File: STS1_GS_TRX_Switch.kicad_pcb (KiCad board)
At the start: 4 copper layers, 101 x 65 mm, 60 parts, among them J1 SDR, J10 PA_Switch, J11 LNA_Switch, J2 From_LNA, J3 To_PA, J4 To_LNA, J5 From_PA, J6 Antenna, J7 RX_LED, J8 TX_LED, J9 5V_Supply, K1 HF3-53, K2 HF3-53, K3 HF3-53, K4 IM07, K5 IM07, Q1 BC847, Q2 BC847, Q3 BC847, Q4 BC847, Q5 BC847, U1 PC817, U2 PC817

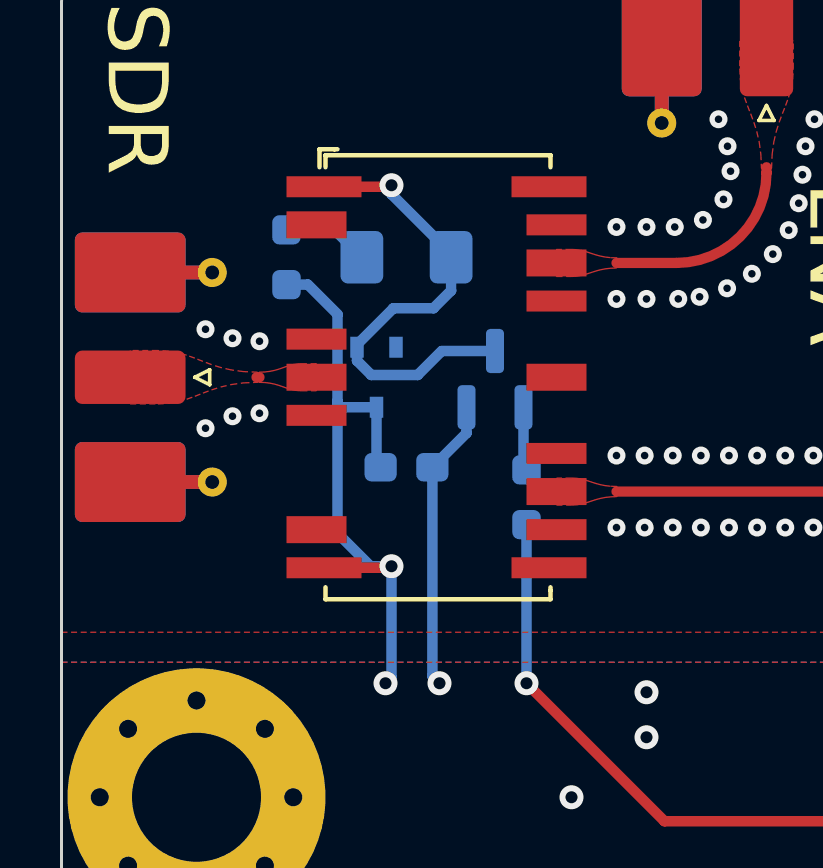
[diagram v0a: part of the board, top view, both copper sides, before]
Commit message: fix: wrong polarity of one of the RF relays
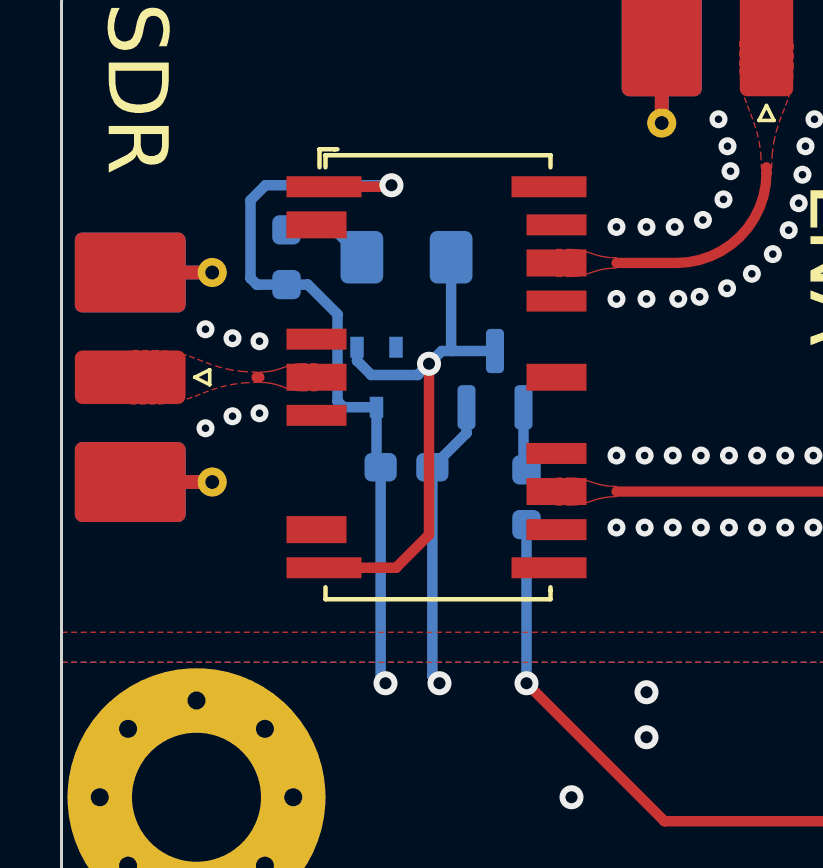
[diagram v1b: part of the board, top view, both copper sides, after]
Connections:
- K1 pad 1: Net-(D1-A) -> +5V
- K1 pad 11: +5V -> Net-(D1-A)
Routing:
- net +5V: track 123.7 -> 128.8 mm
- net Net-(D1-A): track 16.2 -> 18.5 mm

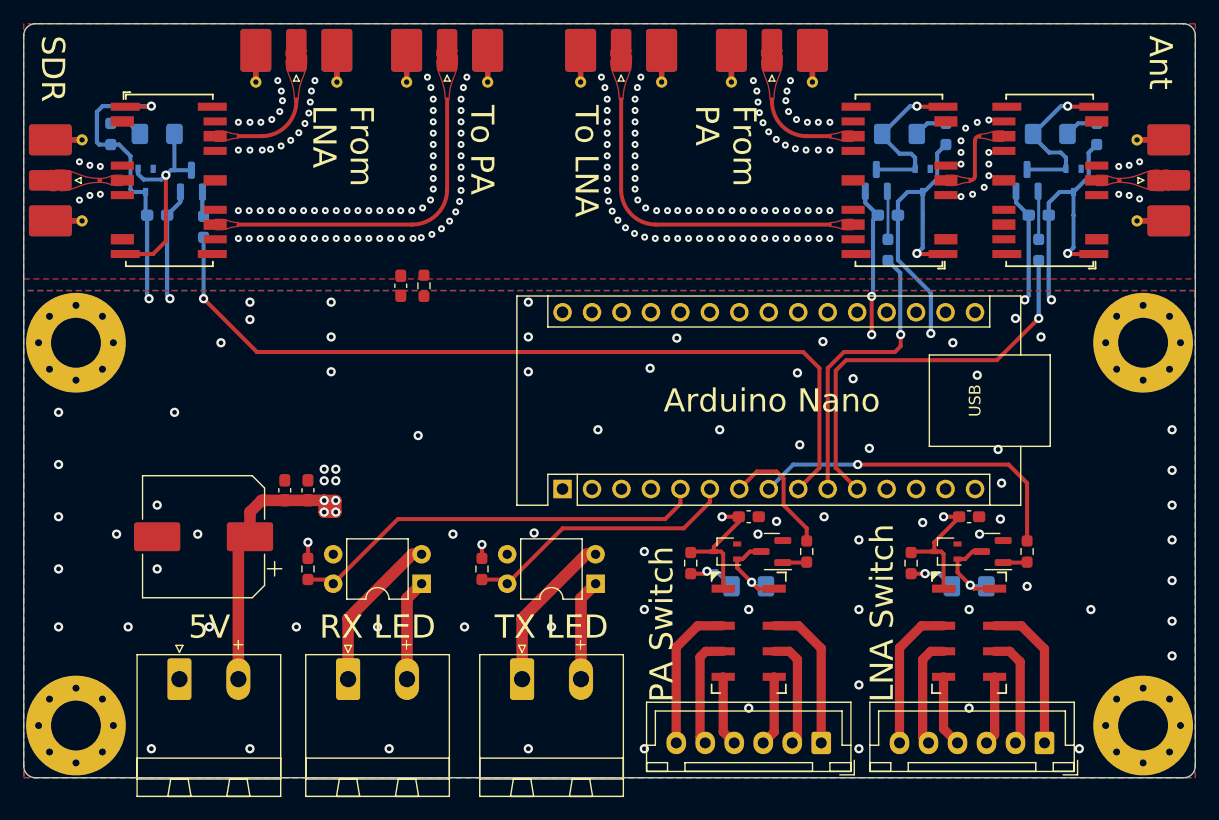
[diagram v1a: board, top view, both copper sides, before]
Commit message: feat: v2.0 with built-in LNA, PA-pre-filter and PA output filter
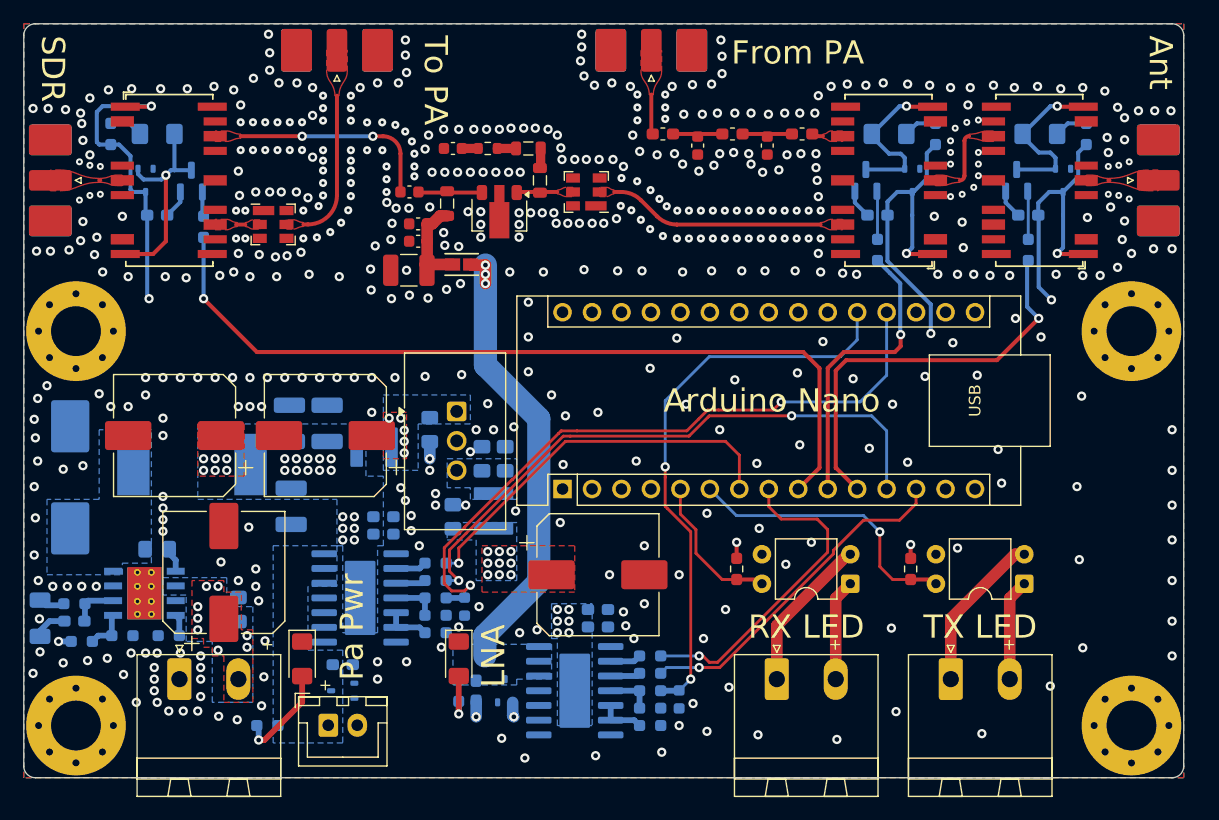
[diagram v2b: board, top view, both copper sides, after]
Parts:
- removed C2: 100µ, Capacitor_SMD:CP_Elec_10x10
- removed C3: 100n, Capacitor_SMD:C_0603_1608Metric_Pad1.08x0.95mm_HandSolder
- removed D10: LNA_Sw, LED_SMD:LED_1206_3216Metric_Pad1.42x1.75mm_HandSolder
- removed J10: PA_Switch, Connector_JST:JST_XH_B6B-XH-A_1x06_P2.50mm_Vertical
- removed J11: LNA_Switch, Connector_JST:JST_XH_B6B-XH-A_1x06_P2.50mm_Vertical
- removed J4: To_LNA, Connector_Coaxial:SMA_Molex_73251-2120_EdgeMount_Horizontal
- removed K4, K5: IM07, Relay_SMD:Relay_DPDT_AXICOM_IMSeries_JLeg
- removed Q4, Q5: BC847, Package_TO_SOT_SMD:SOT-23
- removed R7: 10k, Resistor_SMD:R_0603_1608Metric_Pad0.98x0.95mm_HandSolder
- added C10: 330pF, Capacitor_SMD:C_0603_1608Metric, F.Cu at (144.5, 56.2)
- added C11: 100pF, Capacitor_SMD:C_0603_1608Metric, F.Cu at (141.5, 62.8)
- added C12: 100nF, Capacitor_SMD:C_0603_1608Metric, F.Cu at (141.5, 64.2)
- added C14: 100pF, Capacitor_SMD:C_0603_1608Metric, F.Cu at (140.8, 60.0)
- added C15: 7.5pF, Capacitor_SMD:C_0603_1608Metric, F.Cu at (165.6, 56.0)
- added C16: 7.5pF, Capacitor_SMD:C_0603_1608Metric, F.Cu at (171.6, 56.0)
- added C17: 100pF, Capacitor_SMD:C_0603_1608Metric, B.Cu at (145.5, 95.8)
- added C18: 100pF, Capacitor_SMD:C_0603_1608Metric, B.Cu at (164.0, 103.8)
- added C19: 1µ, Capacitor_SMD:C_0603_1608Metric_Pad1.08x0.95mm_HandSolder, B.Cu at (157.0, 96.0)
- added C20: 1µ, Capacitor_SMD:C_0603_1608Metric_Pad1.08x0.95mm_HandSolder, B.Cu at (157.0, 97.5)
- added C21: 1µ, Capacitor_SMD:C_0603_1608Metric_Pad1.08x0.95mm_HandSolder, B.Cu at (146.5, 103.0)
- added C22: 100µ, Capacitor_SMD:CP_Elec_10x10, F.Cu at (133.5, 81.0)
- added C23: 10µ, Capacitor_SMD:C_0805_2012Metric_Pad1.18x1.45mm_HandSolder, B.Cu at (142.5, 80.5)
- added C24: 10µ, Capacitor_SMD:C_1210_3225Metric_Pad1.33x2.70mm_HandSolder, B.Cu at (130.6, 87.1)
- added C25: 10µ, Capacitor_SMD:C_1210_3225Metric_Pad1.33x2.70mm_HandSolder, B.Cu at (133.7, 80.0)
- added C26: 10µ, Capacitor_SMD:C_0805_2012Metric_Pad1.18x1.45mm_HandSolder, B.Cu at (147.0, 83.0)
- added C27: 10µ, Capacitor_SMD:C_0805_2012Metric_Pad1.18x1.45mm_HandSolder, B.Cu at (149.0, 83.0)
- added C28: 10µ, Capacitor_SMD:C_0805_2012Metric_Pad1.18x1.45mm_HandSolder, B.Cu at (144.5, 88.0)
- added C29: 100µ, Capacitor_SMD:CP_Elec_10x10, F.Cu at (157.0, 93.0)
- added C30: 100µ, Capacitor_SMD:CP_Elec_10x10, F.Cu at (124.8, 92.8)
- added C31: 10µ, Capacitor_SMD:C_0805_2012Metric_Pad1.18x1.45mm_HandSolder, B.Cu at (126.0, 96.0)
- added C32: 100n, Capacitor_SMD:C_0805_2012Metric_Pad1.18x1.45mm_HandSolder, B.Cu at (119.0, 90.8)
- added C33: 100p, Capacitor_SMD:C_0603_1608Metric_Pad1.08x0.95mm_HandSolder, B.Cu at (111.9, 97.0)
- added C34: 7.5n, Capacitor_SMD:C_1206_3216Metric_Pad1.33x1.80mm_HandSolder, B.Cu at (108.9, 96.8)
- added C35: 100µ, Capacitor_SMD:CP_Elec_10x10, F.Cu at (120.5, 81.0)
- added C36: 10µ, Capacitor_SMD:C_1210_3225Metric_Pad1.33x2.70mm_HandSolder, B.Cu at (130.4, 80.0)
- added D11: LNA_Sw, LED_SMD:LED_1206_3216Metric_Pad1.42x1.75mm_HandSolder, F.Cu at (145.0, 100.2)
- added D12: CDBC560-G, Diode_SMD:D_SMC_Handsoldering, B.Cu at (111.5, 84.6)
- added FB1: 600R/0.5A, fbead:Murata-BLM18-0.15-t0.8-0-0-IPC_A, F.Cu at (145.2, 66.2)
- added L1: 33nH, Inductor_SMD:L_0603_1608Metric_Pad1.05x0.95mm_HandSolder, F.Cu at (162.6, 55.0)
- added L2: 51nH, Inductor_SMD:L_0603_1608Metric_Pad1.05x0.95mm_HandSolder, F.Cu at (168.6, 55.0)
- added L3: 220nH, Inductor_SMD:L_0805_2012Metric, F.Cu at (152.0, 59.0)
- added L4: 390nH, Inductor_SMD:L_0805_2012Metric, F.Cu at (151.0, 56.2)
- added L5: 220nH, Inductor_SMD:L_0805_2012Metric, F.Cu at (144.0, 61.0)
- added L6: 33nH, Inductor_SMD:L_0603_1608Metric_Pad1.05x0.95mm_HandSolder, F.Cu at (174.6, 55.0)
- added L7: 5.6µH, Inductor_SMD:L_Abracon_ASPI-4030S, B.Cu at (137.7, 82.0)
- added L8: 5.6µH, Inductor_SMD:L_Abracon_ASPI-4030S, B.Cu at (148.0, 87.5)
- added L9: 27µH, Inductor_SMD:L_Bourns_SRR1210A, B.Cu at (122.0, 83.5)
- added R14: 120, Resistor_SMD:R_0603_1608Metric, F.Cu at (147.5, 56.2)
- added R15: 10k, Resistor_SMD:R_0603_1608Metric_Pad0.98x0.95mm_HandSolder, B.Cu at (143.0, 92.0)
- added R16: 10k, Resistor_SMD:R_0603_1608Metric_Pad0.98x0.95mm_HandSolder, B.Cu at (161.5, 103.0)
- added R17: 10k, Resistor_SMD:R_0603_1608Metric_Pad0.98x0.95mm_HandSolder, B.Cu at (143.0, 93.5)
- added R18: 1.8k, Resistor_SMD:R_0603_1608Metric_Pad0.98x0.95mm_HandSolder, B.Cu at (161.5, 104.5)
- added R19: 10k, Resistor_SMD:R_0603_1608Metric_Pad0.98x0.95mm_HandSolder, B.Cu at (143.0, 95.0)
- added R20: 1.8k, Resistor_SMD:R_0603_1608Metric_Pad0.98x0.95mm_HandSolder, B.Cu at (143.0, 96.5)
- added R21: 10k, Resistor_SMD:R_0603_1608Metric_Pad0.98x0.95mm_HandSolder, B.Cu at (161.5, 106.0)
- added R22: 10k, Resistor_SMD:R_0603_1608Metric_Pad0.98x0.95mm_HandSolder, B.Cu at (145.0, 103.0)
- added R23: 221k, Resistor_SMD:R_0603_1608Metric_Pad0.98x0.95mm_HandSolder, B.Cu at (120.0, 98.2)
- added R24: 221k, Resistor_SMD:R_0603_1608Metric_Pad0.98x0.95mm_HandSolder, B.Cu at (111.9, 95.5)
- added R25: 370k, Resistor_SMD:R_0603_1608Metric_Pad0.98x0.95mm_HandSolder, B.Cu at (112.5, 98.8)
- added R26: 11k, Resistor_SMD:R_0603_1608Metric_Pad0.98x0.95mm_HandSolder, B.Cu at (116.0, 98.2)
- added U3: PGA-103+, Package_TO_SOT_SMD:SOT-89-3, F.Cu at (148.5, 62.0)
- added U4: BTT6050-2EKA, btt6050-2eka:Infineon_PG-DSO-14-40-EP_3.9x8.65mm_P1.27mm, B.Cu at (136.5, 95.0)
- added U5: TSR2-2450, Converter_DCDC:Converter_DCDC_TRACO_TSR2-xxxx_THT, F.Cu at (144.8, 78.9)
- added U6: BTT6050-2EKA, btt6050-2eka:Infineon_PG-DSO-14-40-EP_3.9x8.65mm_P1.27mm, B.Cu at (155.0, 103.0)
- added U7: TPS54360DDA, Package_SO:TI_SO-PowerPAD-8_ThermalVias, B.Cu at (117.9, 94.6)
- added X1: SF2446E, saw:Filter_SAW-6_3.0x3.0mm, F.Cu at (156.0, 60.0)
- added X2: SF2446E, saw:Filter_SAW-6_3.0x3.0mm, F.Cu at (129.0, 62.8)
- C1: value 1µ -> 10µ; footprint Capacitor_SMD:C_0603_1608Metric_Pad1.08x0.95mm_HandSolder -> Capacitor_SMD:C_1210_3225Metric_Pad1.33x2.70mm_HandSolder
- C7, C8, C9, D4, D5, R6: moved to B.Cu
- D9: moved to F.Cu
- J1, J3, J5, J6: footprint Connector_Coaxial:SMA_Molex_73251-2120_EdgeMount_Horizontal -> SMA:SMA_Molex_73251-2120_EdgeMount_Horizontal
- J2: value From_LNA -> PA_Pwr; footprint Connector_Coaxial:SMA_Molex_73251-2120_EdgeMount_Horizontal -> Connector_JST:JST_XH_B2B-XH-A_1x02_P2.50mm_Vertical
- J9: value 5V_Supply -> 48V_Supply
- R13: value 1M -> 10k; moved to B.Cu
- R8, R9: value 1k -> 10k; moved to B.Cu
- moved J2 58.5 mm to (133.8, 106.0), turned to 0 degrees
- moved D4 53.4 mm to (135.0, 103.0)
- moved C8 50.5 mm to (138.5, 89.5)
- moved R6 39.1 mm to (128.5, 106.0), turned to 0 degrees
- moved D9 39.0 mm to (131.5, 100.2), turned to -90 degrees
- moved R13 38.7 mm to (161.5, 101.5), turned to 180 degrees
- moved R1 37.0 mm to (184.0, 92.5)
- moved R2 37.0 mm to (169.0, 92.5)
- moved J7 37.0 mm to (172.4, 102.0)
- moved J8 37.0 mm to (187.4, 102.0)
- moved U1 37.0 mm to (178.8, 93.8)
- moved U2 37.0 mm to (193.8, 93.8)
- moved R9 33.7 mm to (161.5, 100.0), turned to 180 degrees
- moved C9 33.0 mm to (135.0, 100.8), turned to 0 degrees
- moved R8 32.8 mm to (143.0, 98.0), turned to 180 degrees
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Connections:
- A1 pad 12: unconnected-(A1-D9-Pad12) -> /FET_PA_DEN
- A1 pad 13: unconnected-(A1-D10-Pad13) -> /FET_LNA_DEN
- A1 pad 19: unconnected-(A1-A0-Pad19) -> /FET_PA_IS
- A1 pad 20: unconnected-(A1-A1-Pad20) -> /FET_LNA_IS
- C1 pad 1: +5V -> GND
- C1 pad 2: GND -> Net-(C1-Pad2)
- C7 pad 1: +5V -> +30V
- C8 pad 1: +5V -> +30V
- C9 pad 1: GNDA -> /PA_PWR
- D4 pad 1: Net-(D10-K) -> GND
- D4 pad 3: +5V -> /PA_PWR
- D5 pad 1: Net-(D5-A) -> GND
- D5 pad 3: +5V -> /LNA_PWR
- D9 pad 1: Net-(D5-A) -> GND
- J1 pad 2: GNDA -> GND
- J2 pad 1: /RF_From_LNA -> /PA_PWR
- J2 pad 2: GNDA -> GND
- J3 pad 2: GNDA -> GND
- J5 pad 2: GNDA -> GND
- J6 pad 2: GNDA -> GND
- J9 pad 2: +5V -> +48V
- K1 pad 10: GNDA -> GND
- K1 pad 12: GNDA -> GND
- K1 pad 13: GNDA -> GND
- K1 pad 14: /RF_To_PA -> /RF_To_PA_Prefilter
- K1 pad 15: GNDA -> GND
- K1 pad 17: GNDA -> GND
- K1 pad 19: GNDA -> GND
- K1 pad 2: GNDA -> GND
- K1 pad 21: GNDA -> GND
- K1 pad 22: GNDA -> GND
- K1 pad 5: GNDA -> GND
- K1 pad 7: GNDA -> GND
- K2 pad 10: GNDA -> GND
- K2 pad 12: GNDA -> GND
- K2 pad 13: GNDA -> GND
- K2 pad 14: /RF_From_PA -> /RF_From_LPF
- K2 pad 15: GNDA -> GND
- K2 pad 17: GNDA -> GND
- K2 pad 19: GNDA -> GND
- K2 pad 2: GNDA -> GND
- K2 pad 21: GNDA -> GND
- K2 pad 22: GNDA -> GND
- K2 pad 5: GNDA -> GND
- K2 pad 7: GNDA -> GND
- K3 pad 10: GNDA -> GND
- K3 pad 12: GNDA -> GND
- K3 pad 13: GNDA -> GND
- K3 pad 15: GNDA -> GND
- K3 pad 17: GNDA -> GND
- K3 pad 19: GNDA -> GND
- K3 pad 2: GNDA -> GND
- K3 pad 20: GNDA -> GND
- K3 pad 21: GNDA -> GND
- K3 pad 22: GNDA -> GND
- K3 pad 5: GNDA -> GND
- K3 pad 7: GNDA -> GND
- R13 pad 1: GNDA -> /FET_LNA_DEN
- R13 pad 2: GND -> Net-(U6-DEN)
- R6 pad 2: +5V -> /PA_PWR
- R8 pad 1: Net-(Q4-B) -> GND
- R8 pad 2: /PA_Sw_Out -> Net-(U4-DSEL)
- R9 pad 1: Net-(Q5-B) -> /LNA_Sw_Out
- R9 pad 2: /LNA_Sw_Out -> Net-(U6-IN0)
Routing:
- net /FET_PA_IS: track 0.00 -> 58.4 mm, vias 0 -> 2
- net /FET_PA_DEN: track 0.00 -> 52.1 mm, vias 0 -> 2
- net /FET_LNA_IS: track 0.00 -> 49.0 mm, vias 0 -> 2
- net +5V: track 128.8 -> 81.6 mm, vias 14 -> 23
- net /LNA_PWR: track 0.00 -> 40.4 mm, vias 0 -> 3
- net /FET_LNA_DEN: track 0.00 -> 29.5 mm, vias 0 -> 1
- net +30V: track 0.00 -> 25.8 mm, vias 0 -> 23
- net /~{RX_En_In}: track 36.4 -> 12.9 mm
- net /PA_Sw_Out: track 10.9 -> 33.8 mm, vias 0 -> 1
- net GND: track 32.8 -> 14.6 mm, vias 82 -> 511
- net /RF_To_PA: track 27.4 -> 12.8 mm
- net Net-(J11-Pin_1): track 13.2 -> 0.00 mm
- net Net-(J10-Pin_6): track 13.1 -> 0.00 mm
- net Net-(J10-Pin_1): track 13.0 -> 0.00 mm
- net Net-(J11-Pin_6): track 12.8 -> 0.00 mm
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- added copper zone on B.Cu, net +30V
- added copper zone on F.Cu, net +30V
- added copper zone on In2.Cu, net +30V
- added copper zone on B.Cu, net +48V
- added copper zone on F.Cu, net +48V
- added copper zone on B.Cu, net +5V
- added copper zone on F.Cu, net +5V
- added copper zone on In2.Cu, net +5V
- added copper zone on B.Cu, net /LNA_PWR
- added copper zone on B.Cu, net /PA_PWR
- added copper zone on F.Cu, net /RF_From_LPF
- added copper zone on F.Cu, net /RF_LNA2
- added copper zone on F.Cu, net /RF_To_PA_Prefilter
- added copper zone on B.Cu, net /TPS_Sw
- added copper zone on B.Cu, net /TRS_Post
- added copper zone on B.Cu, net /TRS_Pre
- added copper zone on F.Cu, net /TRS_Pre
- added copper zone on In1.Cu, net GND
- removed copper zone on In1.Cu, net +5V
- removed copper zone on F.Cu, net GNDA
- removed copper zone on In1.Cu, net GNDA
- removed copper zone on In2.Cu, net GNDA
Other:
- board size 101 x 65 mm -> 100 x 65 mm
- board text added: "LNA"
- board text added: "Pa Pwr"
- board text added: "STS1 TRX Switch v2.0"
- board text removed: "5V"
- board text removed: "From LNA"
- board text removed: "LNA Power"
- board text removed: "LNA Switch"
- board text removed: "PA Power"
- board text removed: "PA Switch"
- board text removed: "STS1 TRX Switch v1.0"
- board text removed: "To LNA"
